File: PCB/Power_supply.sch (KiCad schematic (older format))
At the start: 30 parts

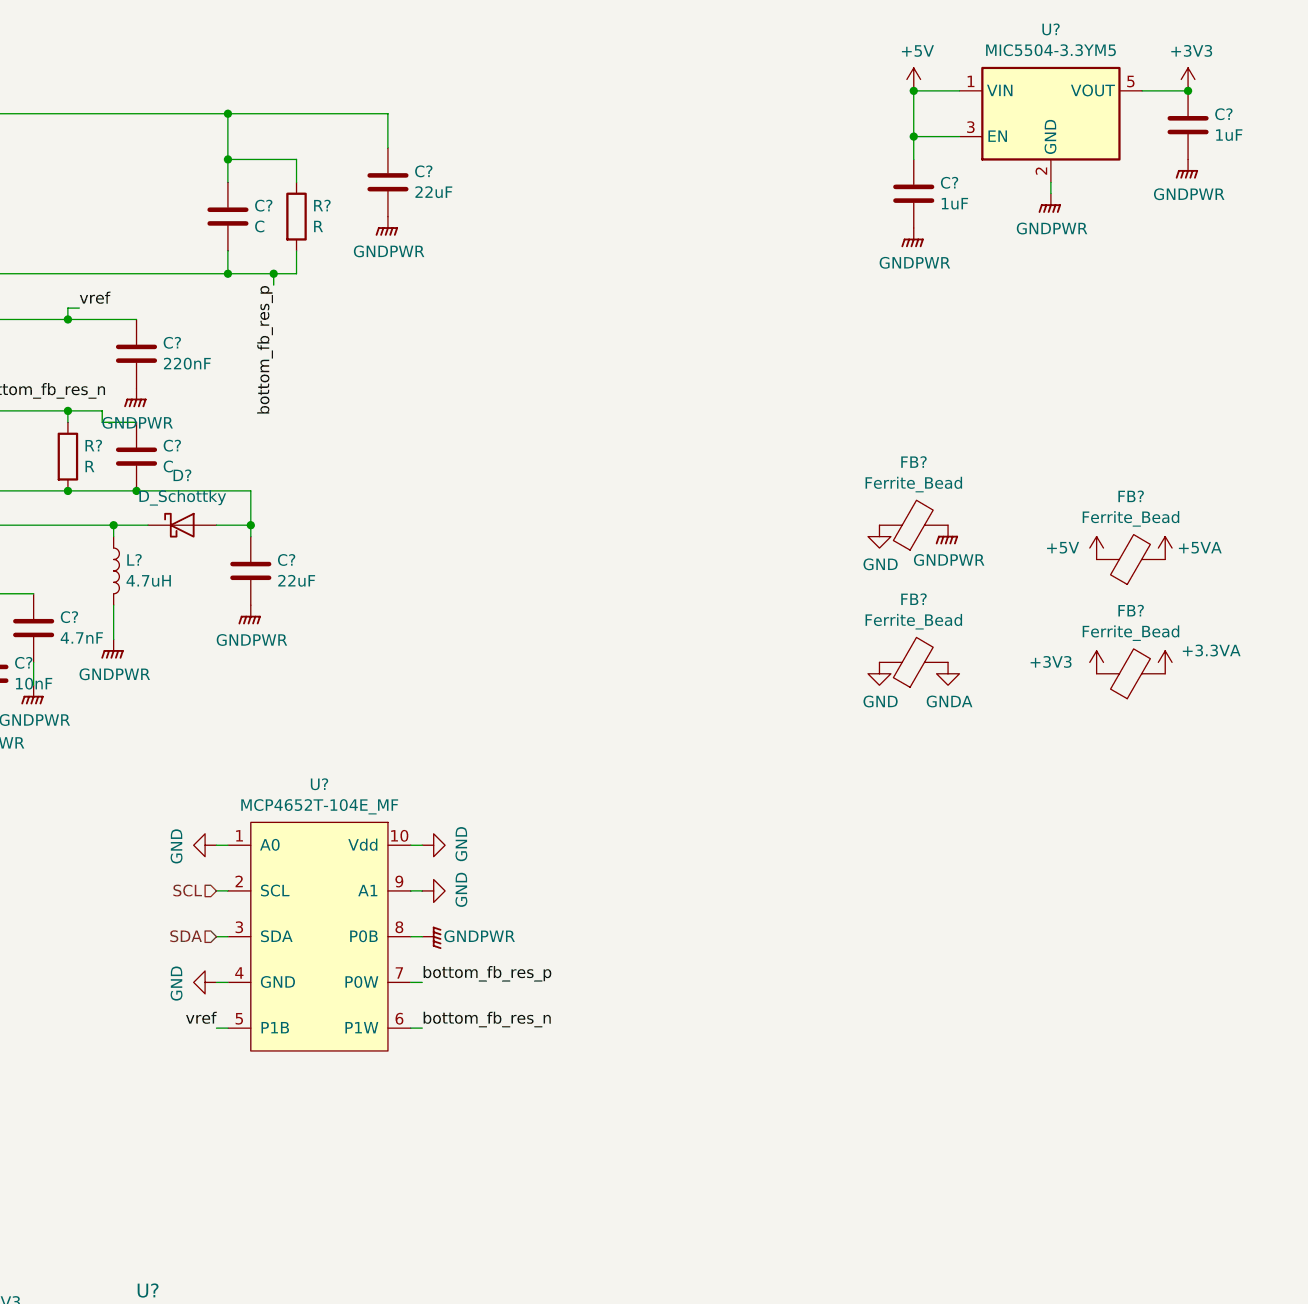
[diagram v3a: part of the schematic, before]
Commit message: Advancement in schematic regarding oscilloscope and power supply
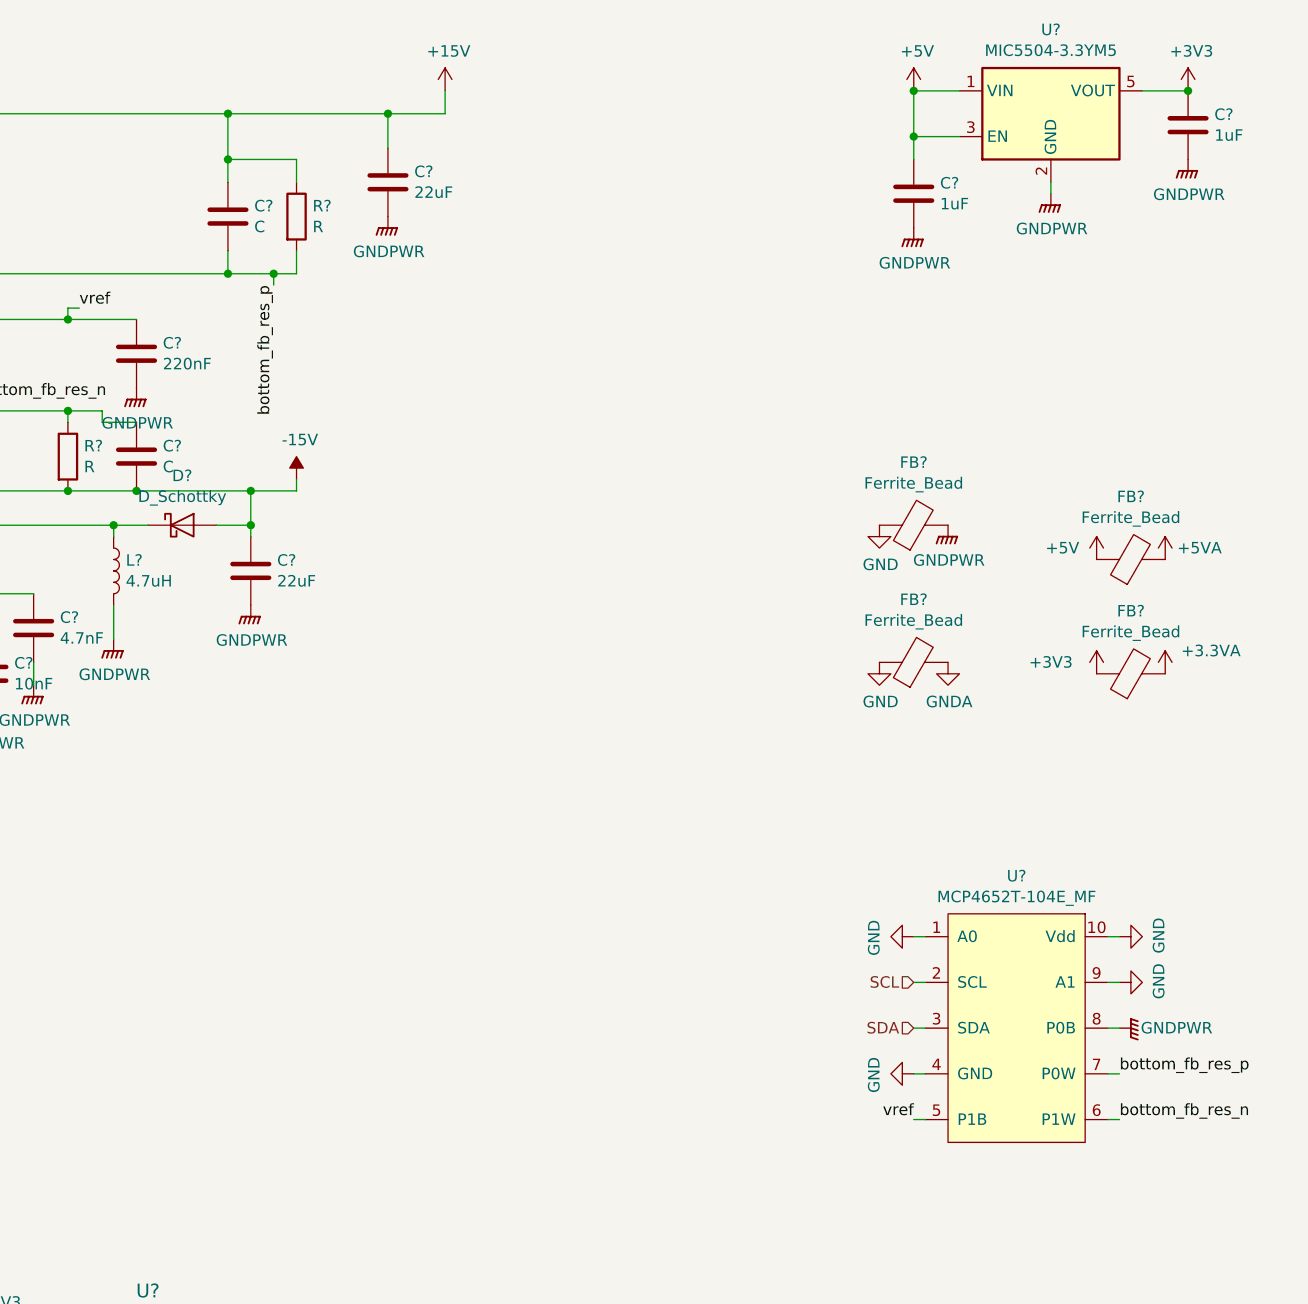
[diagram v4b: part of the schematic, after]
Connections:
- net -15V: now reaches C?.1, C?.2, D?.2 (A), R?.2, U?.15 (VNEG)
- net +15V: now reaches C?.1, C?.1, D?.1 (K), R?.1, U?.23 (VPOS)
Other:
- moved on the sheet: U?
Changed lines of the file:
@@
 L power:GNDPWR #PWR?
 U 1 1 5E95802B
-P 6300 4950
-F 0 "#PWR?" H 6300 4750 50  0001 C CNN
-F 1 "GNDPWR" V 6300 4700 50  0000 C CNN
-F 2 "" H 6300 4900 50  0001 C CNN
-F 3 "" H 6300 4900 50  0001 C CNN
-	1    6300 4950
+P 9350 5350
+F 0 "#PWR?" H 9350 5150 50  0001 C CNN
+F 1 "GNDPWR" V 9350 5100 50  0000 C CNN
+F 2 "" H 9350 5300 50  0001 C CNN
+F 3 "" H 9350 5300 50  0001 C CNN
+	1    9350 5350
 	0    -1   -1   0
 $EndComp
@@
 L power:GND #PWR?
 U 1 1 5E95DE30
-P 5400 5150
-F 0 "#PWR?" H 5400 4900 50  0001 C CNN
-F 1 "GND" H 5405 4977 50  0000 C CNN
-F 2 "" H 5400 5150 50  0001 C CNN
-F 3 "" H 5400 5150 50  0001 C CNN
-	1    5400 5150
+P 8450 5550
+F 0 "#PWR?" H 8450 5300 50  0001 C CNN
+F 1 "GND" H 8455 5377 50  0000 C CNN
+F 2 "" H 8450 5550 50  0001 C CNN
+F 3 "" H 8450 5550 50  0001 C CNN
+	1    8450 5550
 	0    1    1    0
 $EndComp
@@
 L power:GND #PWR?
 U 1 1 5E96015B
-P 5400 4550
-F 0 "#PWR?" H 5400 4300 50  0001 C CNN
-F 1 "GND" H 5405 4377 50  0000 C CNN
-F 2 "" H 5400 4550 50  0001 C CNN
-F 3 "" H 5400 4550 50  0001 C CNN
-	1    5400 4550
+P 8450 4950
+F 0 "#PWR?" H 8450 4700 50  0001 C CNN
+F 1 "GND" H 8455 4777 50  0000 C CNN
+F 2 "" H 8450 4950 50  0001 C CNN
+F 3 "" H 8450 4950 50  0001 C CNN
+	1    8450 4950
 	0    1    1    0
 $EndComp
@@
 L MCP46X1:MCP4652T-104E_MF U?
 U 1 1 5E9570D9
-P 5850 4350
-F 0 "U?" H 5850 4415 50  0000 C CNN
-F 1 "MCP4652T-104E_MF" H 5850 4324 50  0000 C CNN
-F 2 "" H 5850 4350 50  0001 C CNN
-F 3 "" H 5850 4350 50  0001 C CNN
-	1    5850 4350
+P 8900 4750
+F 0 "U?" H 8900 4815 50  0000 C CNN
+F 1 "MCP4652T-104E_MF" H 8900 4724 50  0000 C CNN
+F 2 "" H 8900 4750 50  0001 C CNN
+F 3 "" H 8900 4750 50  0001 C CNN
+	1    8900 4750
 	1    0    0    -1
 $EndComp
@@
 L power:GND #PWR?
 U 1 1 5E9625EE
-P 6300 4750
-F 0 "#PWR?" H 6300 4500 50  0001 C CNN
-F 1 "GND" H 6305 4577 50  0000 C CNN
-F 2 "" H 6300 4750 50  0001 C CNN
-F 3 "" H 6300 4750 50  0001 C CNN
-	1    6300 4750
+P 9350 5150
+F 0 "#PWR?" H 9350 4900 50  0001 C CNN
+F 1 "GND" H 9355 4977 50  0000 C CNN
+F 2 "" H 9350 5150 50  0001 C CNN
+F 3 "" H 9350 5150 50  0001 C CNN
+	1    9350 5150
 	0    -1   -1   0
 $EndComp
 Wire Wire Line
-	6250 4750 6300 4750
-Wire Wire Line
-	6250 4950 6300 4950
-Wire Wire Line
-	5400 4550 5450 4550
-Wire Wire Line
-	5400 5150 5450 5150
-Wire Wire Line
-	5400 5350 5450 5350
+	9300 5150 9350 5150
+Wire Wire Line
+	9300 5350 9350 5350
+Wire Wire Line
+	8450 4950 8500 4950
+Wire Wire Line
+	8450 5550 8500 5550
+Wire Wire Line
+	8450 5750 8500 5750
 Wire Wire Line
 	2100 6550 2050 6550
@@
 Wire Wire Line
 	2050 6750 2100 6750
-Text HLabel 5400 4750 0    50   Input ~ 0
+Text HLabel 8450 5150 0    50   Input ~ 0
 SCL
-Text HLabel 5400 4950 0    50   Input ~ 0
+Text HLabel 8450 5350 0    50   Input ~ 0
 SDA
 Wire Wire Line
-	5400 4950 5450 4950
-Wire Wire Line
-	5400 4750 5450 4750
+	8450 5350 8500 5350
+Wire Wire Line
+	8450 5150 8500 5150
 $Comp
 L power:GND #PWR?
 U 1 1 5E9AEB53
-P 6300 4550
-F 0 "#PWR?" H 6300 4300 50  0001 C CNN
-F 1 "GND" H 6305 4377 50  0000 C CNN
-F 2 "" H 6300 4550 50  0001 C CNN
-F 3 "" H 6300 4550 50  0001 C CNN
-	1    6300 4550
+P 9350 4950
+F 0 "#PWR?" H 9350 4700 50  0001 C CNN
+F 1 "GND" H 9355 4777 50  0000 C CNN
+F 2 "" H 9350 4950 50  0001 C CNN
+F 3 "" H 9350 4950 50  0001 C CNN
+	1    9350 4950
 	0    -1   -1   0
 $EndComp
 Wire Wire Line
-	6250 4550 6300 4550
-Wire Wire Line
-	6250 5150 6300 5150
-Wire Wire Line
-	6250 5350 6300 5350
+	9300 4950 9350 4950
+Wire Wire Line
+	9300 5550 9350 5550
+Wire Wire Line
+	9300 5750 9350 5750
 Wire Wire Line
 	5650 2050 5650 2100
@@
 Text Label 4800 2200 0    50   ~ 0
 vref
-Text Label 5400 5350 2    50   ~ 0
+Text Label 8450 5750 2    50   ~ 0
 vref
-Text Label 6300 5150 0    50   ~ 0
+Text Label 9350 5550 0    50   ~ 0
 bottom_fb_res_p
-Text Label 6300 5350 0    50   ~ 0
+Text Label 9350 5750 0    50   ~ 0
 bottom_fb_res_n
 Text Label 4350 2600 0    50   ~ 0
@@
 Text HLabel 2400 3900 0    50   Input ~ 0
 power_switch_enable
+$Comp
+L power:+15V #PWR?
+U 1 1 5EA29880
+P 6400 1250
+F 0 "#PWR?" H 6400 1100 50  0001 C CNN
+F 1 "+15V" H 6415 1423 50  0000 C CNN
+F 2 "" H 6400 1250 50  0001 C CNN
+F 3 "" H 6400 1250 50  0001 C CNN
+	1    6400 1250
+	1    0    0    -1
+$EndComp
+$Comp
+L power:-15V #PWR?
+U 1 1 5EA2C1AB
+P 5750 2950
+F 0 "#PWR?" H 5750 3050 50  0001 C CNN
+F 1 "-15V" H 5765 3123 50  0000 C CNN
+F 2 "" H 5750 2950 50  0001 C CNN
+F 3 "" H 5750 2950 50  0001 C CNN
+	1    5750 2950
+	1    0    0    -1
+$EndComp
+Wire Wire Line
+	6150 1350 6400 1350
+Wire Wire Line
+	6400 1350 6400 1250
+Connection ~ 6150 1350
+Wire Wire Line
+	5550 3000 5750 3000
+Wire Wire Line
+	5750 3000 5750 2950
+Connection ~ 5550 3000
 $EndSCHEMATC
